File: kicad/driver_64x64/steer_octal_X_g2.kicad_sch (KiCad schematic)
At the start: 66 parts

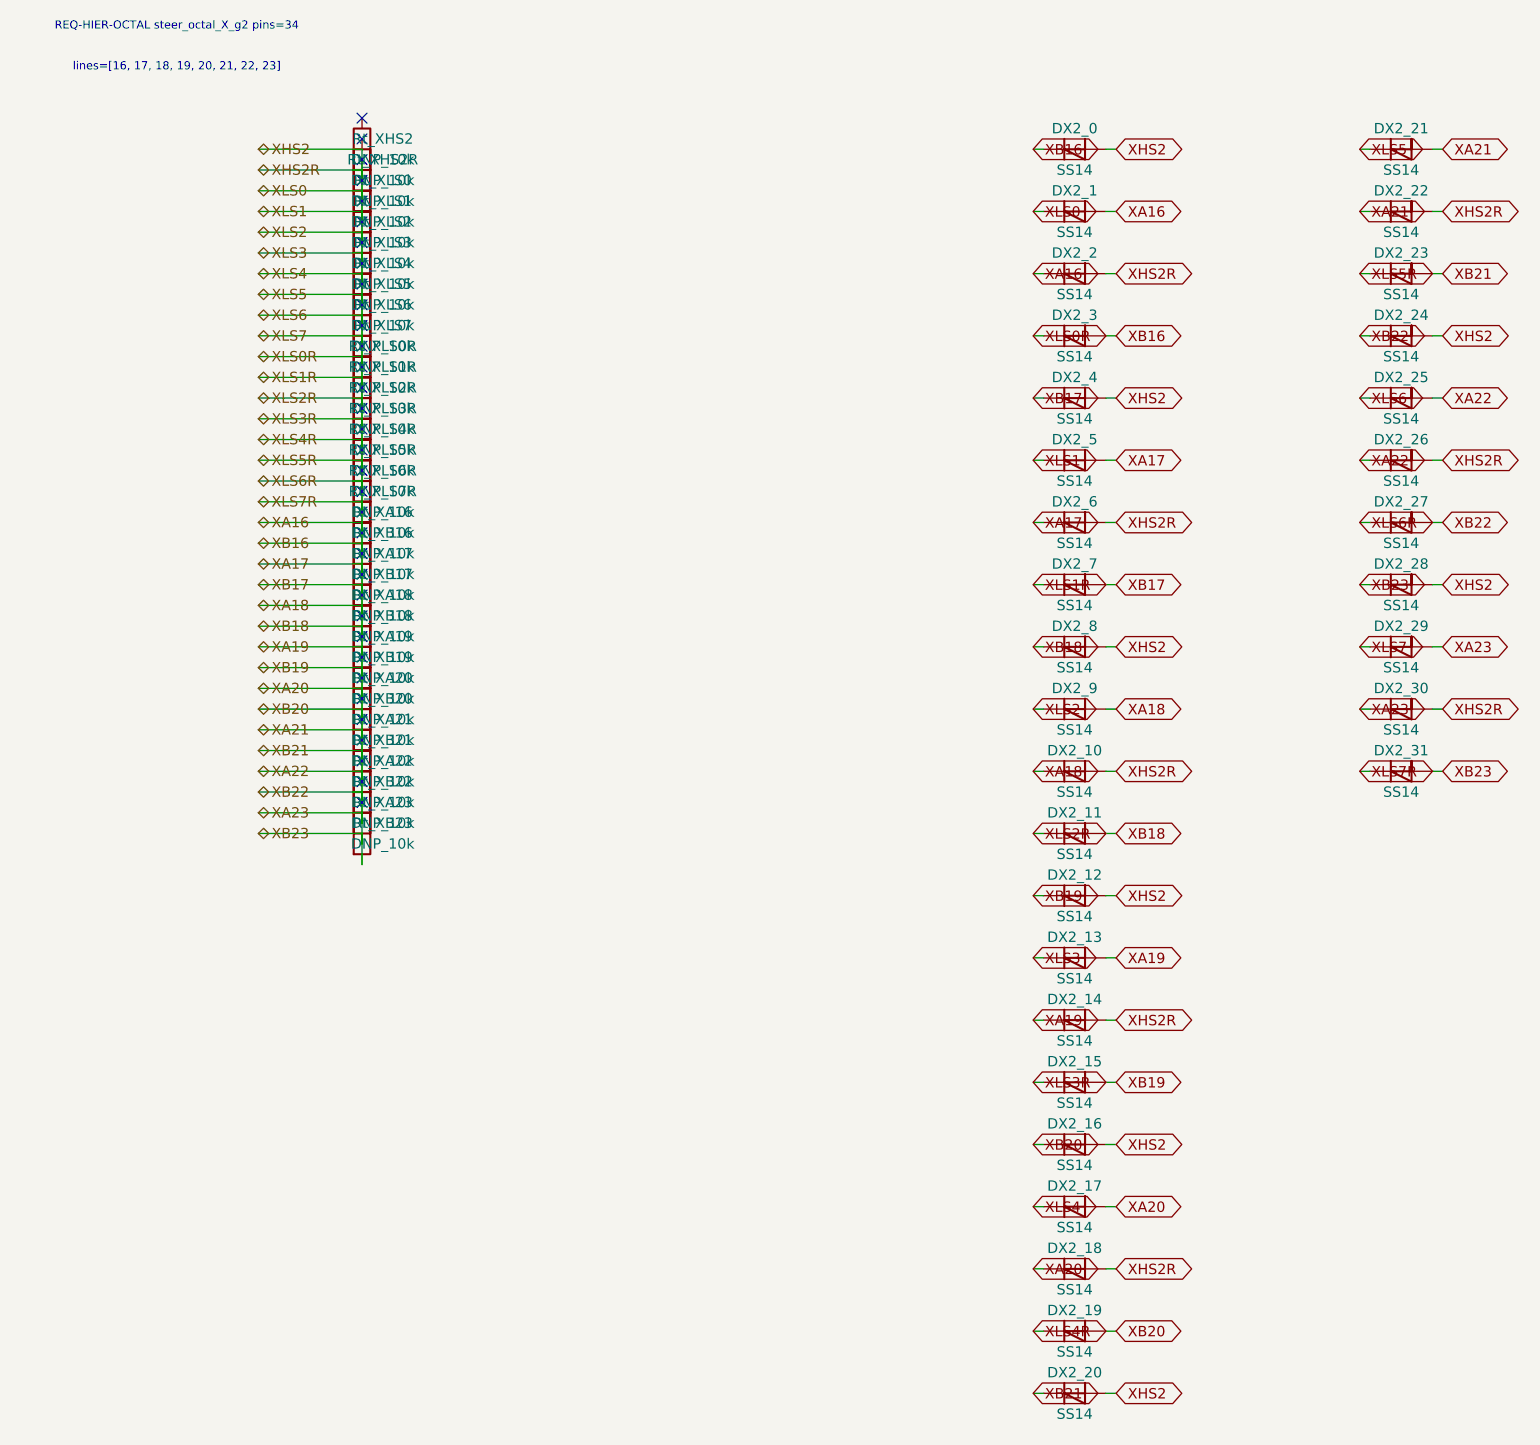
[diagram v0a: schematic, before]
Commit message: logical seperation into host and multiple decode/drive/steering boards
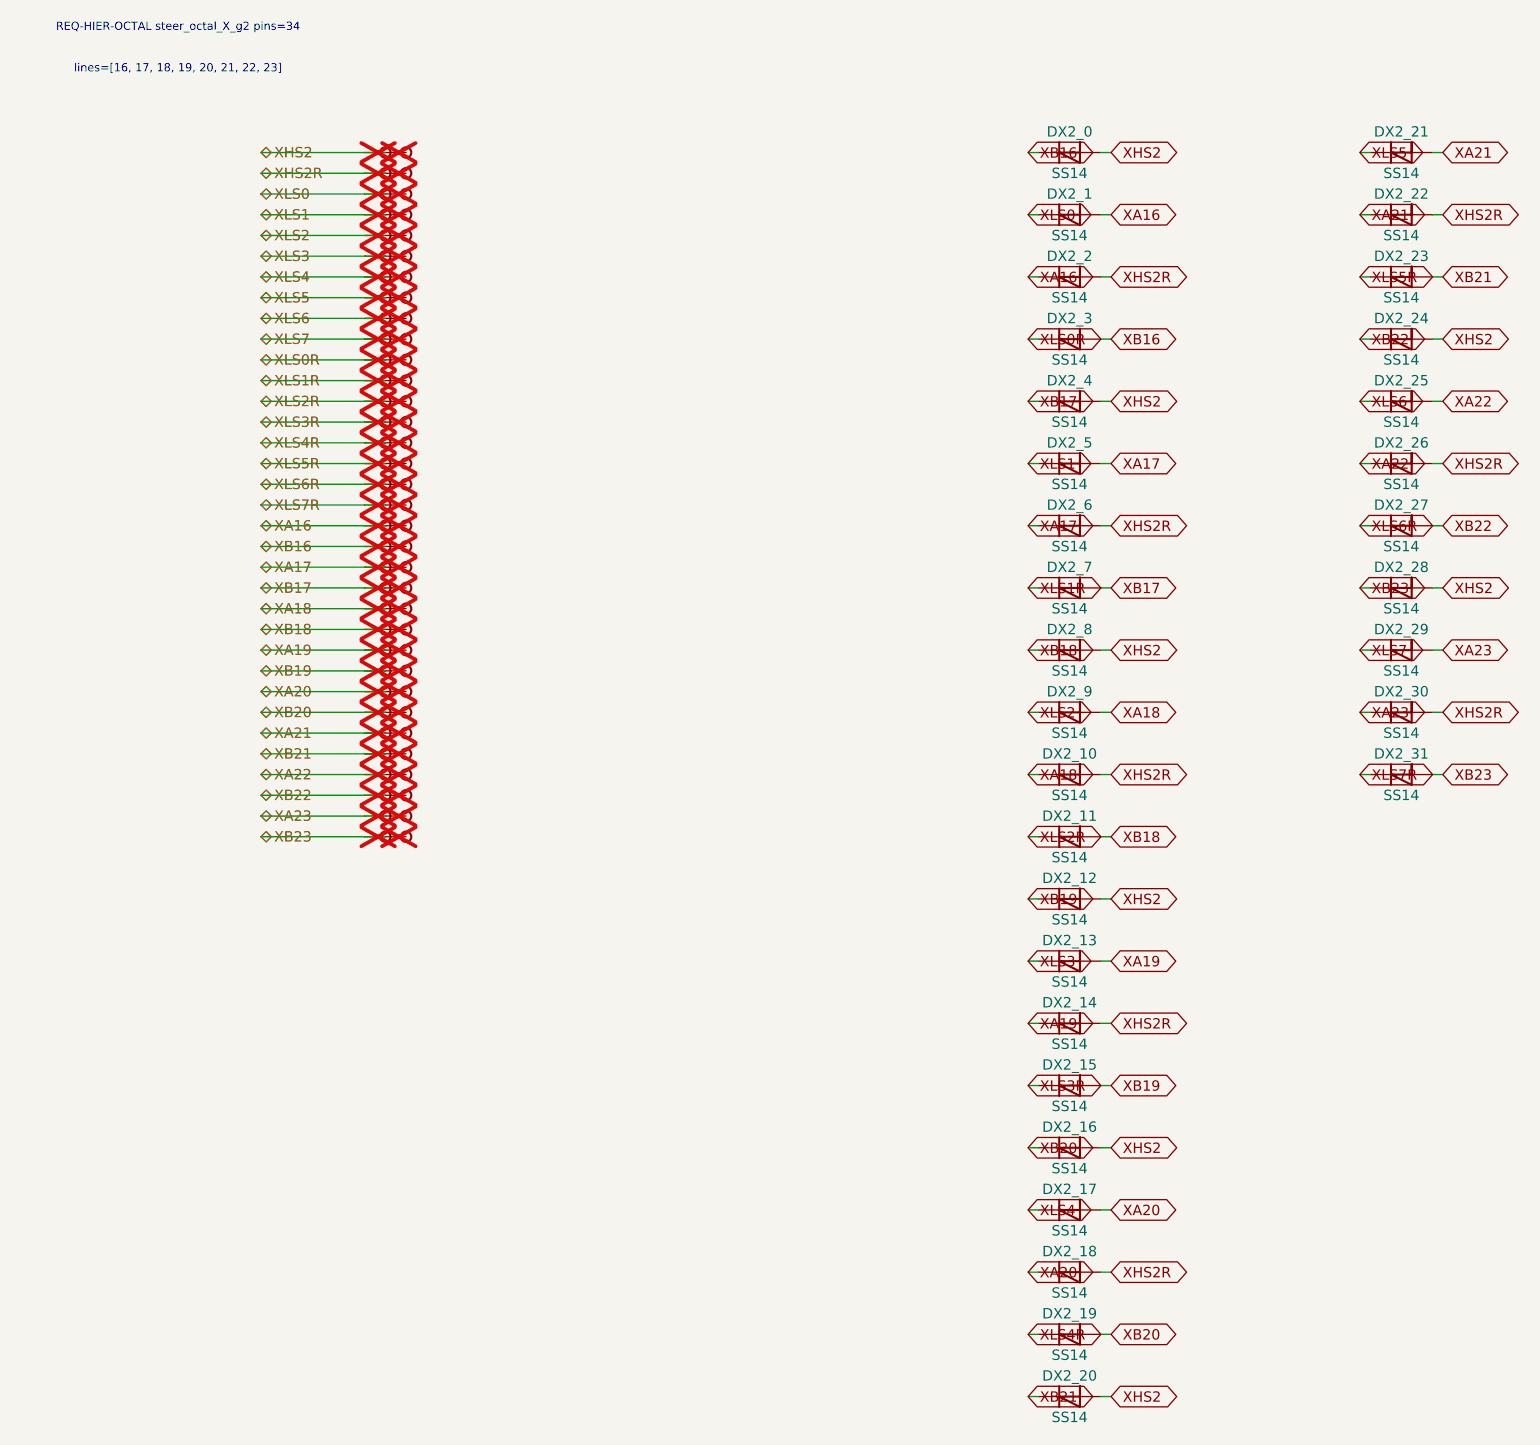
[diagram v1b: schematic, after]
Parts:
- removed Rt_XA16, Rt_XA17, Rt_XA18, Rt_XA19, Rt_XA20, Rt_XA21, Rt_XA22, Rt_XA23, Rt_XB16, Rt_XB17, Rt_XB18, Rt_XB19, Rt_XB20, Rt_XB21, Rt_XB22, Rt_XB23, Rt_XHS2, Rt_XHS2R, Rt_XLS0, Rt_XLS0R, Rt_XLS1, Rt_XLS1R, Rt_XLS2, Rt_XLS2R, Rt_XLS3, Rt_XLS3R, Rt_XLS4, Rt_XLS4R, Rt_XLS5, Rt_XLS5R, Rt_XLS6, Rt_XLS6R, Rt_XLS7, Rt_XLS7R: DNP_10k, symbol Device:R
- added TP_XA16, TP_XA16b, TP_XA17, TP_XA17b, TP_XA18, TP_XA18b, TP_XA19, TP_XA19b, TP_XA20, TP_XA20b, TP_XA21, TP_XA21b, TP_XA22, TP_XA22b, TP_XA23, TP_XA23b, TP_XB16, TP_XB16b, TP_XB17, TP_XB17b, TP_XB18, TP_XB18b, TP_XB19, TP_XB19b, TP_XB20, TP_XB20b, TP_XB21, TP_XB21b, TP_XB22, TP_XB22b, TP_XB23, TP_XB23b, TP_XHS2, TP_XHS2R, TP_XHS2Rb, TP_XHS2b, TP_XLS0, TP_XLS0R, TP_XLS0Rb, TP_XLS0b, TP_XLS1, TP_XLS1R, TP_XLS1Rb, TP_XLS1b, TP_XLS2, TP_XLS2R, TP_XLS2Rb, TP_XLS2b, TP_XLS3, TP_XLS3R, TP_XLS3Rb, TP_XLS3b, TP_XLS4, TP_XLS4R, TP_XLS4Rb, TP_XLS4b, TP_XLS5, TP_XLS5R, TP_XLS5Rb, TP_XLS5b, TP_XLS6, TP_XLS6R, TP_XLS6Rb, TP_XLS6b, TP_XLS7, TP_XLS7R, TP_XLS7Rb, TP_XLS7b: Stub, symbol CMR:Stub
- DX2_0, DX2_1, DX2_10, DX2_11, DX2_12, DX2_13, DX2_14, DX2_15, DX2_16, DX2_17, DX2_18, DX2_19, DX2_2, DX2_20, DX2_21, DX2_22, DX2_23, DX2_24, DX2_25, DX2_26, DX2_27, DX2_28, DX2_29, DX2_3, DX2_30, DX2_31, DX2_4, DX2_5, DX2_6, DX2_7, DX2_8, DX2_9: symbol Device:D_Schottky -> CMR:D_Schottky
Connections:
- net XA16: now also TP_XA16.1, TP_XA16b.1; no longer DX2_0.1 (K), DX2_0.2 (A), DX2_1.1 (K), DX2_10.1 (K), DX2_10.2 (A), DX2_11.1 (K), DX2_11.2 (A), DX2_12.1 (K), DX2_12.2 (A), DX2_13.1 (K), DX2_13.2 (A), DX2_14.1 (K), DX2_14.2 (A), DX2_15.1 (K), DX2_15.2 (A), DX2_16.1 (K), DX2_16.2 (A), DX2_17.1 (K), DX2_17.2 (A), DX2_18.1 (K), DX2_18.2 (A), DX2_19.1 (K), DX2_19.2 (A), DX2_2.2 (A), DX2_20.1 (K), DX2_20.2 (A), DX2_21.1 (K), DX2_21.2 (A), DX2_22.1 (K), DX2_22.2 (A), DX2_23.1 (K), DX2_23.2 (A), DX2_24.1 (K), DX2_24.2 (A), DX2_25.1 (K), DX2_25.2 (A), DX2_26.1 (K), DX2_26.2 (A), DX2_27.1 (K), DX2_27.2 (A), DX2_28.1 (K), DX2_28.2 (A), DX2_29.1 (K), DX2_29.2 (A), DX2_3.1 (K), DX2_3.2 (A), DX2_30.1 (K), DX2_30.2 (A), DX2_31.1 (K), DX2_31.2 (A), DX2_4.1 (K), DX2_4.2 (A), DX2_5.1 (K), DX2_5.2 (A), DX2_6.1 (K), DX2_6.2 (A), DX2_7.1 (K), DX2_7.2 (A), DX2_8.1 (K), DX2_8.2 (A), DX2_9.1 (K), DX2_9.2 (A)
- new net XA17: DX2_5.2 (A), DX2_6.1 (K), TP_XA17.1, TP_XA17b.1
- new net XA18: DX2_10.1 (K), DX2_9.2 (A), TP_XA18.1, TP_XA18b.1
- new net XA19: DX2_13.2 (A), DX2_14.1 (K), TP_XA19.1, TP_XA19b.1
- new net XA20: DX2_17.2 (A), DX2_18.1 (K), TP_XA20.1, TP_XA20b.1
- new net XA21: DX2_21.2 (A), DX2_22.1 (K), TP_XA21.1, TP_XA21b.1
- new net XA22: DX2_25.2 (A), DX2_26.1 (K), TP_XA22.1, TP_XA22b.1
- new net XA23: DX2_29.2 (A), DX2_30.1 (K), TP_XA23.1, TP_XA23b.1
- new net XB16: DX2_0.1 (K), DX2_3.2 (A), TP_XB16.1, TP_XB16b.1
- new net XB17: DX2_4.1 (K), DX2_7.2 (A), TP_XB17.1, TP_XB17b.1
- new net XB18: DX2_11.2 (A), DX2_8.1 (K), TP_XB18.1, TP_XB18b.1
- new net XB19: DX2_12.1 (K), DX2_15.2 (A), TP_XB19.1, TP_XB19b.1
- new net XB20: DX2_16.1 (K), DX2_19.2 (A), TP_XB20.1, TP_XB20b.1
- new net XB21: DX2_20.1 (K), DX2_23.2 (A), TP_XB21.1, TP_XB21b.1
- new net XB22: DX2_24.1 (K), DX2_27.2 (A), TP_XB22.1, TP_XB22b.1
- new net XB23: DX2_28.1 (K), DX2_31.2 (A), TP_XB23.1, TP_XB23b.1
- new net XHS2: DX2_0.2 (A), DX2_12.2 (A), DX2_16.2 (A), DX2_20.2 (A), DX2_24.2 (A), DX2_28.2 (A), DX2_4.2 (A), DX2_8.2 (A), TP_XHS2.1, TP_XHS2b.1
- new net XHS2R: DX2_10.2 (A), DX2_14.2 (A), DX2_18.2 (A), DX2_2.2 (A), DX2_22.2 (A), DX2_26.2 (A), DX2_30.2 (A), DX2_6.2 (A), TP_XHS2R.1, TP_XHS2Rb.1
- new net XLS0: DX2_1.1 (K), TP_XLS0.1, TP_XLS0b.1
- new net XLS0R: DX2_3.1 (K), TP_XLS0R.1, TP_XLS0Rb.1
- new net XLS1: DX2_5.1 (K), TP_XLS1.1, TP_XLS1b.1
- new net XLS1R: DX2_7.1 (K), TP_XLS1R.1, TP_XLS1Rb.1
- new net XLS2: DX2_9.1 (K), TP_XLS2.1, TP_XLS2b.1
- new net XLS2R: DX2_11.1 (K), TP_XLS2R.1, TP_XLS2Rb.1
- new net XLS3: DX2_13.1 (K), TP_XLS3.1, TP_XLS3b.1
- new net XLS3R: DX2_15.1 (K), TP_XLS3R.1, TP_XLS3Rb.1
- new net XLS4: DX2_17.1 (K), TP_XLS4.1, TP_XLS4b.1
- new net XLS4R: DX2_19.1 (K), TP_XLS4R.1, TP_XLS4Rb.1
- new net XLS5: DX2_21.1 (K), TP_XLS5.1, TP_XLS5b.1
- new net XLS5R: DX2_23.1 (K), TP_XLS5R.1, TP_XLS5Rb.1
- new net XLS6: DX2_25.1 (K), TP_XLS6.1, TP_XLS6b.1
- new net XLS6R: DX2_27.1 (K), TP_XLS6R.1, TP_XLS6Rb.1
- new net XLS7: DX2_29.1 (K), TP_XLS7.1, TP_XLS7b.1
- new net XLS7R: DX2_31.1 (K), TP_XLS7R.1, TP_XLS7Rb.1
- no-connect marks 34 -> 0
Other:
- moved on the sheet: DX2_0, DX2_1, DX2_10, DX2_11, DX2_12, DX2_13, DX2_14, DX2_15, DX2_16, DX2_17, DX2_18, DX2_19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
